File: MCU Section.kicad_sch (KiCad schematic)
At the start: 81 parts, among them J2 Conn_02x03_Odd_Even, J3 Conn_01x04, U10 ESP32-C6-MINI-1-H8, U11 TLV62569ADRL, U12 XAL4020-222MEB, U13 GD25Q256EYIGR, U18 ESD5451N_C2936977, U8 ESD5451N_C2936977, U9 ESP32-P4NRW32_C22387510, X1 XXDBBCNANF-40.000000MHZ

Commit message: Done with the correction, PCB is complete
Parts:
- removed C42: 10uF, Capacitor_SMD:C_0805_2012Metric, symbol Device:C_Small
- added C14: 22pF, PCM_JLCPCB:C_0402, symbol PCM_JLCPCB-Capacitors:0402,22pF
- added C15: 22uF, PCM_JLCPCB:C_0603, symbol PCM_JLCPCB-Capacitors:0603,22uF
- R13, R14: value 100k -> 499k; LCSC C25803 -> (none)
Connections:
- net VDDO_FLASH is gone; now on net VDD_FLASH: C62.1, U9.71 (VFB/VO1)
- net C6_U0RXD: now also U9.60 (GPIO30)
- net C6_U0TXD: now also U9.61 (GPIO31)
- net ESP_VDD_HP: now also C14.1, C15.1
- net FB_DCDC: now also C14.2
- net GND: now also C15.2
- net SDB: now also U9.18 (GPIO17)
- net ALERT: now reaches U9.19 (GPIO18)
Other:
- note added: "1.2 = 0.6*(1+R13/499)"
- note added: "R13=499k"
- note removed: "1.2 = 0.6*(1+R13/100)"
- note removed: "R13=100k"

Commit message: Corrected the issues raised
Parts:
- added R56, R57: 0Ω, PCM_JLCPCB:R_0402, symbol PCM_JLCPCB-Resistors:0402,0Ω
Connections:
- net DSI_DATA0_N: now also U9.40 (DSI_DATAN0); no longer U9.39 (DSI_DATAP0)
- net DSI_DATA0_P: now also U9.39 (DSI_DATAP0); no longer U9.40 (DSI_DATAN0)
- net ESP_3V3: now also R57.1
- net VDD_FLASH: now also R56.2, R57.2; no longer C62.1, U9.71 (VFB/VO1)
- net LCD_RESET: now reaches U9.56 (GPIO27)
- new net ESP_LDO_VO1: C62.1, R56.1, U9.71 (VFB/VO1)
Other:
- moved on the sheet: C40, C44, C96, C97, R4, RST1, RST2, U18, U8

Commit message: Prepare the production files, Included the 3D rendering images
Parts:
- C39, C48: LCSC (none) -> C15195
- C93, C94: LCSC (none) -> C1549
- H10, H11, H12, H13, H2, H3, H5, H6, H7, H8, H9: now not fitted
- R13, R14: LCSC Part (none) -> C131054
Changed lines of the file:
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@@
 		(on_board yes)
 		(in_pos_files yes)
-		(dnp no)
+		(dnp yes)
 		(fields_autoplaced yes)
 		(property "Reference" "H12"
@@
 			)
 		)
+		(property "LCSC" "C1549"
+			(at 314.96 208.28 0)
+			(hide yes)
+			(show_name no)
+			(do_not_autoplace no)
+			(effects
+				(font
+					(size 1.27 1.27)
+				)
+			)
+		)
 		(pin "2"
 		)
@@
 		(on_board yes)
 		(in_pos_files yes)
-		(dnp no)
+		(dnp yes)
 		(fields_autoplaced yes)
 		(property "Reference" "H3"
@@
 		(on_board yes)
 		(in_pos_files yes)
-		(dnp no)
+		(dnp yes)
 		(fields_autoplaced yes)
 		(property "Reference" "H6"
@@
 			)
 		)
-		(property "LCSC" ""
+		(property "LCSC Part" "C131054"
 			(at 142.24 82.55 0)
 			(hide yes)
@@
 		(on_board yes)
 		(in_pos_files yes)
-		(dnp no)
+		(dnp yes)
 		(fields_autoplaced yes)
 		(property "Reference" "H7"
@@
 			)
 		)
+		(property "LCSC" "C15195"
+			(at 171.45 350.52 0)
+			(hide yes)
+			(show_name no)
+			(do_not_autoplace no)
+			(effects
+				(font
+					(size 1.27 1.27)
+				)
+			)
+		)
 		(pin "2"
 		)
@@
 			)
 		)
+		(property "LCSC" "C1549"
+			(at 340.36 208.28 0)
+			(hide yes)
+			(show_name no)
+			(do_not_autoplace no)
+			(effects
+				(font
+					(size 1.27 1.27)
+				)
+			)
+		)
 		(pin "2"
 		)
@@
 		(on_board yes)
 		(in_pos_files yes)
-		(dnp no)
+		(dnp yes)
 		(fields_autoplaced yes)
 		(property "Reference" "H13"
@@
 			)
 		)
+		(property "LCSC" "C15195"
+			(at 175.26 325.12 0)
+			(hide yes)
+			(show_name no)
+			(do_not_autoplace no)
+			(effects
+				(font
+					(size 1.27 1.27)
+				)
+			)
+		)
 		(pin "2"
 		)
@@
 		(on_board yes)
 		(in_pos_files yes)
-		(dnp no)
+		(dnp yes)
 		(fields_autoplaced yes)
 		(property "Reference" "H9"
@@
 		(on_board yes)
 		(in_pos_files yes)
-		(dnp no)
+		(dnp yes)
 		(fields_autoplaced yes)
 		(property "Reference" "H10"
@@
 		(on_board yes)
 		(in_pos_files yes)
-		(dnp no)
+		(dnp yes)
 		(fields_autoplaced yes)
 		(property "Reference" "H5"
@@
 		(on_board yes)
 		(in_pos_files yes)
-		(dnp no)
+		(dnp yes)
 		(fields_autoplaced yes)
 		(property "Reference" "H11"
@@
 			)
 		)
-		(property "LCSC" ""
+		(property "LCSC Part" "C131054"
 			(at 142.24 74.93 0)
 			(hide yes)
@@
 		(on_board yes)
 		(in_pos_files yes)
-		(dnp no)
+		(dnp yes)
 		(fields_autoplaced yes)
 		(property "Reference" "H2"
@@
 		(on_board yes)
 		(in_pos_files yes)
-		(dnp no)
+		(dnp yes)
 		(fields_autoplaced yes)
 		(property "Reference" "H8"

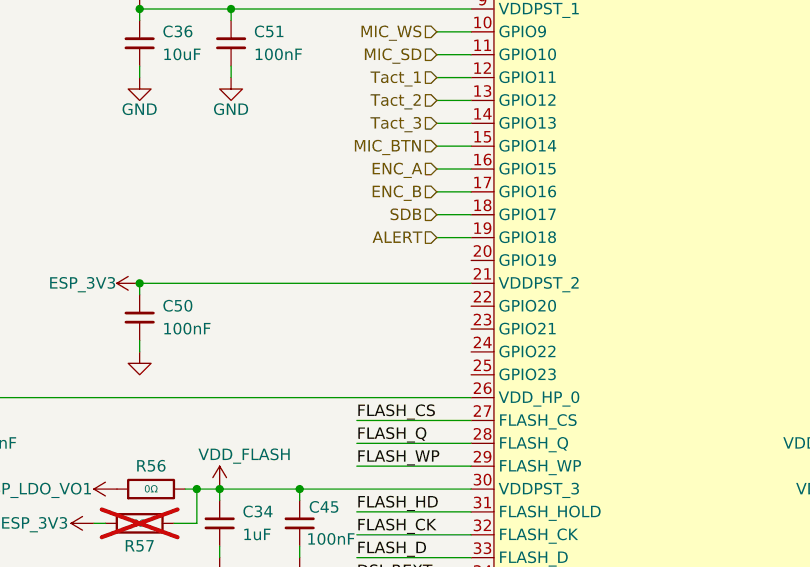
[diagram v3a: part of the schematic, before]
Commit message: Added GT911 connector and fix the USB_C issue
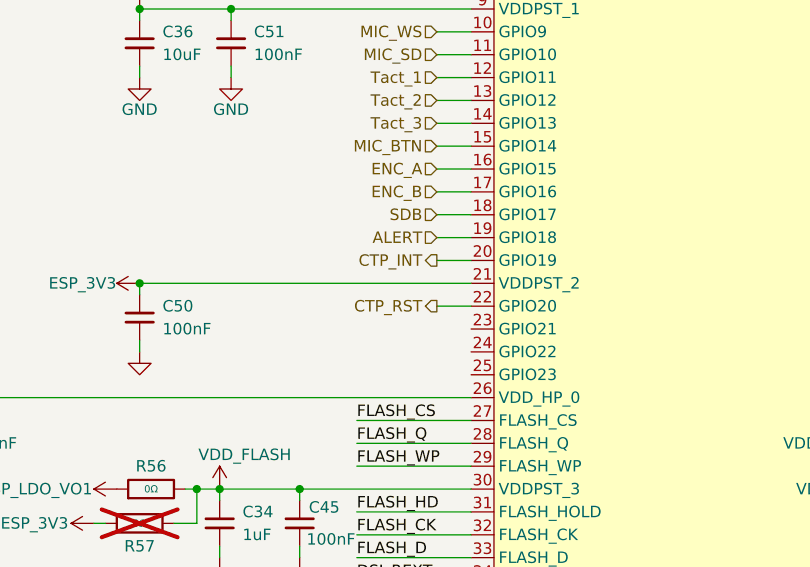
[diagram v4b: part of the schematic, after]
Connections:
- net CTP_INT: now reaches U9.20 (GPIO19)
- net CTP_RST: now reaches U9.22 (GPIO20)
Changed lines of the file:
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@@
+	(wire
+		(pts
+			(xy 189.23 267.97) (xy 193.04 267.97)
+		)
+		(stroke
+			(width 0)
+			(type default)
+		)
+	)
 	(wire
 		(pts
@@
 		(pts
 			(xy 189.23 260.35) (xy 193.04 260.35)
+		)
+		(stroke
+			(width 0)
+			(type default)
+		)
+	)
+	(wire
+		(pts
+			(xy 189.23 273.05) (xy 193.04 273.05)
 		)
 		(stroke
@@
 		)
 	)
+	(hierarchical_label "CTP_RST"
+		(shape output)
+		(at 189.23 273.05 180)
+		(effects
+			(font
+				(size 1.27 1.27)
+			)
+			(justify right)
+		)
+	)
 	(hierarchical_label "DSI_DATA0_P"
 		(shape output)
@@
 		(effects
 			(font
+				(size 1.27 1.27)
+			)
+			(justify right)
+		)
+	)
+	(hierarchical_label "CTP_INT"
+		(shape output)
+		(at 189.23 267.97 180)
+		(effects
+			(font

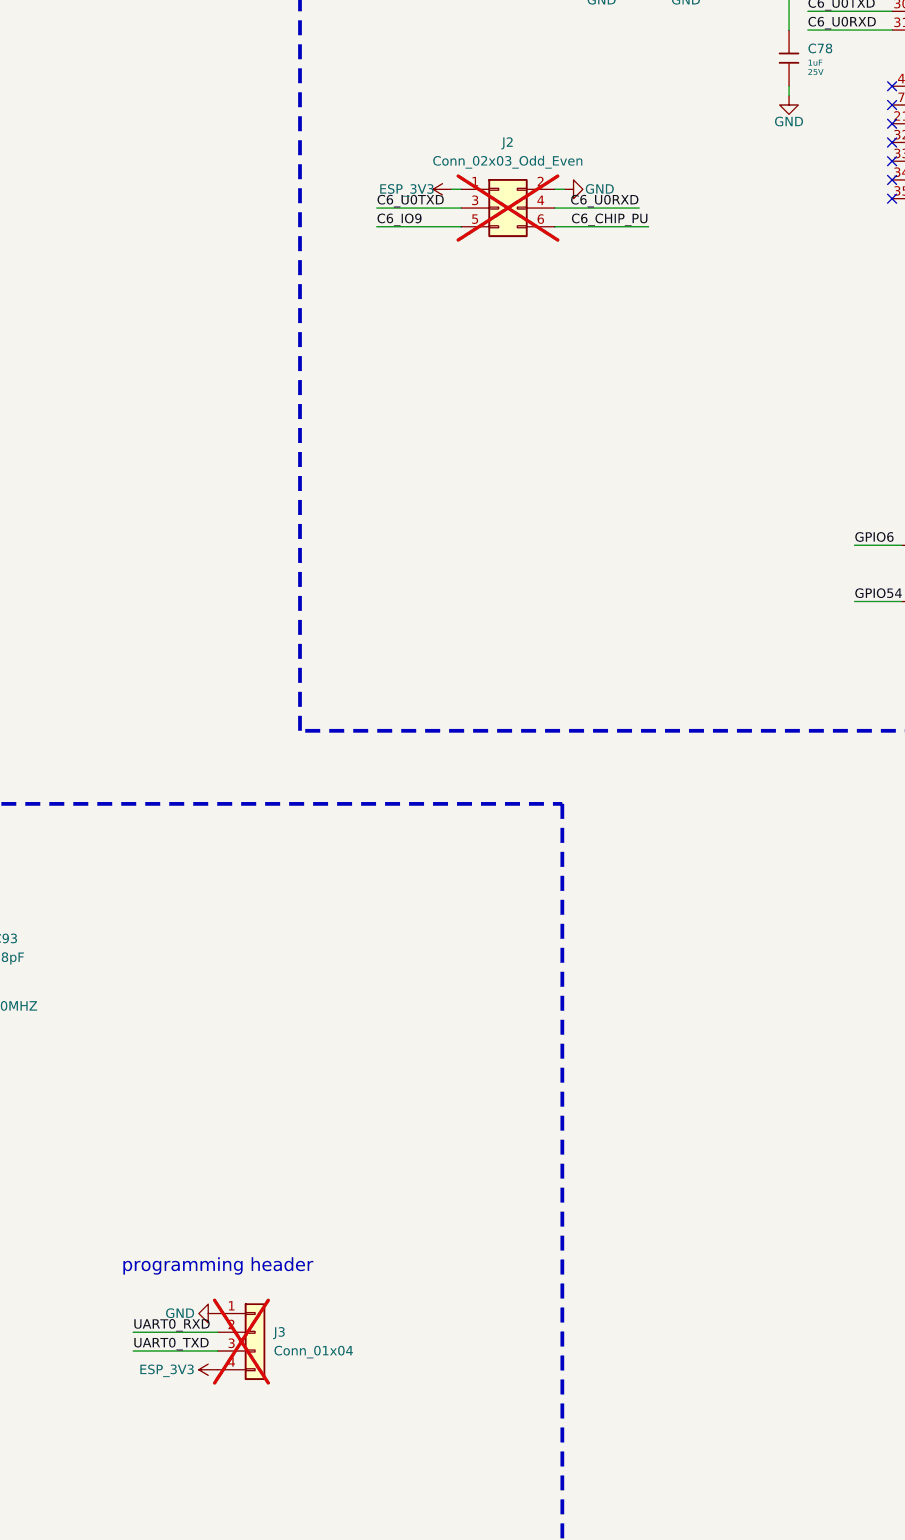
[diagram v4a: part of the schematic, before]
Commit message: Added the connector and generated updated production files
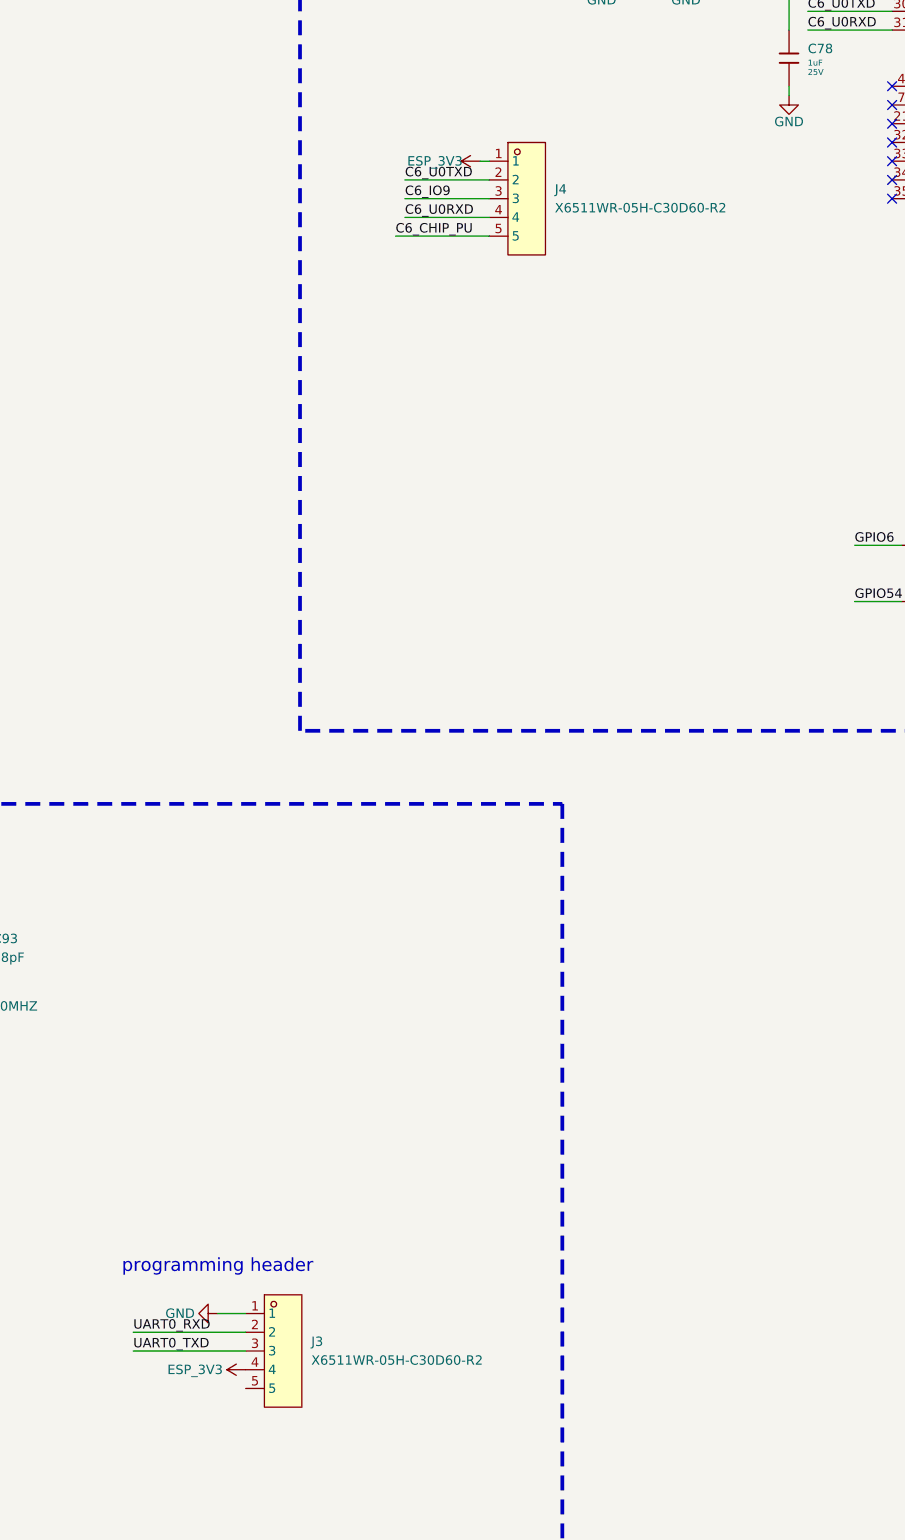
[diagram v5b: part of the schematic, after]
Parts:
- removed J2: Conn_02x03_Odd_Even, Connector_PinHeader_2.54mm:PinHeader_2x03_P2.54mm_Vertical, symbol Connector_Generic:Conn_02x03_Odd_Even
- removed J3: Conn_01x04, Connector_PinHeader_2.54mm:PinHeader_1x04_P2.54mm_Vertical, symbol Connector_Generic:Conn_01x04
- added J3, J4: X6511WR-05H-C30D60-R2, X6511WR-05H-C60D30R2:HDR-TH_5P-P2.54-H-M-W10.4, symbol X6511WR-05H-C60D30R2:X6511WR-05H-C30D60-R2
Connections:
- net C6_CHIP_PU: now also J4.5
- net C6_IO9: now also J4.3
- net C6_U0RXD: now also J4.4
- net C6_U0TXD: now also J4.2
- net ESP_3V3: now also J3.4, J4.1
- net GND: now also J3.1
- net UART0_RXD: now also J3.2
- net UART0_TXD: now also J3.3
